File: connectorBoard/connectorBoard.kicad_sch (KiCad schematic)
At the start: 6 parts, among them J1 Conn_01x08_Female

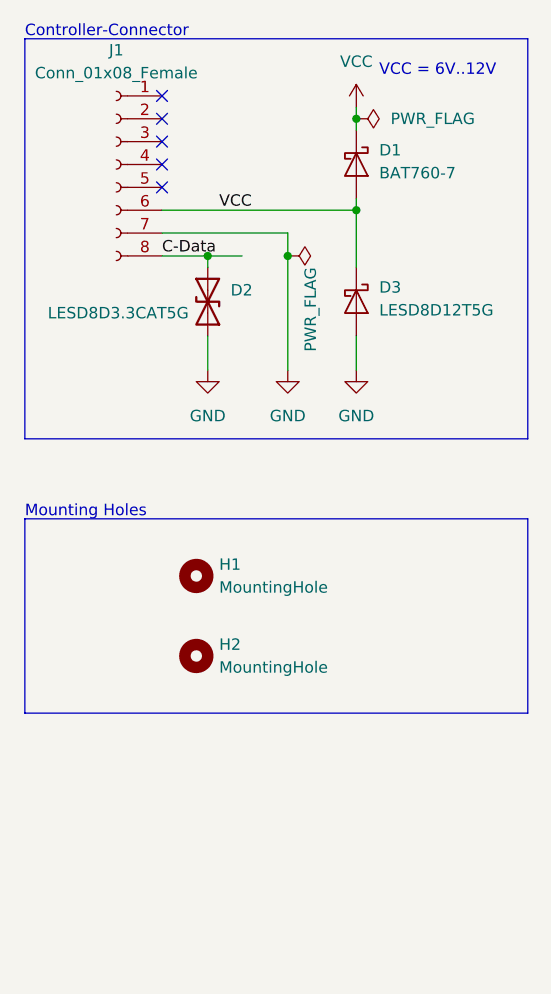
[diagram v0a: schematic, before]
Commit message: basic connector pcb design
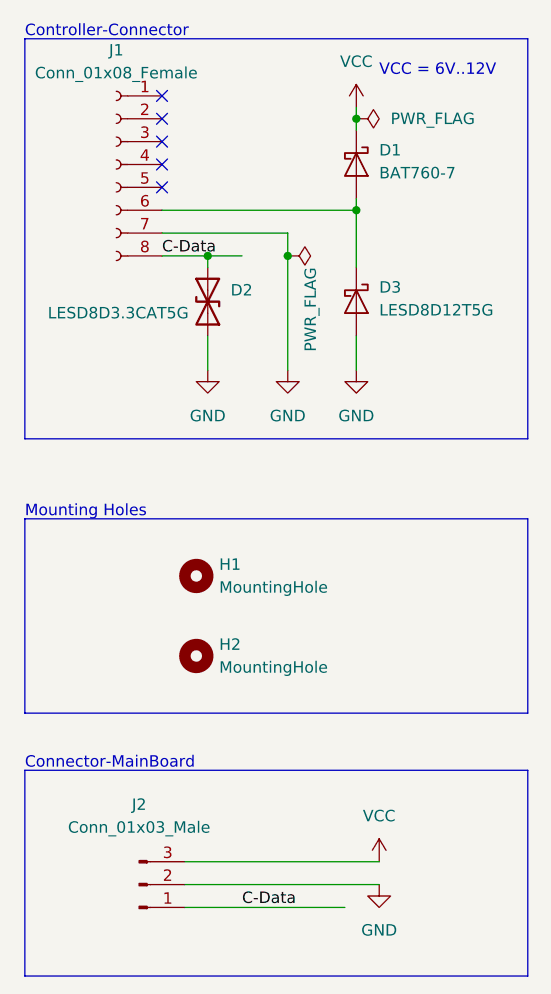
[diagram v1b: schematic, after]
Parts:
- added J2: Conn_01x03_Male, Connector_JST:JST_GH_SM03B-GHS-TB_1x03-1MP_P1.25mm_Horizontal, symbol Connector:Conn_01x03_Male
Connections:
- net C-Data: now also J2.1 (Pin_1)
- net GND: now also J2.2 (Pin_2)
- net VCC: now also J2.3 (Pin_3); no longer D1.2 (A), D3.1 (K), J1.6 (Pin_6)
- new net: D1.2 (A), D3.1 (K), J1.6 (Pin_6)
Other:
- note added: "Connector-MainBoard"
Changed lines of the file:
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@@
+    (stroke (width 0) (type default) (color 0 0 0 0))
+  )
+  (polyline (pts (xy 21.59 125.73) (xy 77.47 125.73))
     (stroke (width 0) (type default) (color 0 0 0 0))
   )
@@
     (stroke (width 0) (type default) (color 0 0 0 0))
   )
+  (polyline (pts (xy 77.47 125.73) (xy 77.47 102.87))
+    (stroke (width 0) (type default) (color 0 0 0 0))
+  )
   (wire (pts (xy 36.83 40.64) (xy 58.42 40.64))
     (stroke (width 0) (type default) (color 0 0 0 0))
   )
+  (wire (pts (xy 39.37 115.57) (xy 60.96 115.57))
+    (stroke (width 0) (type default) (color 0 0 0 0))
+  )
+  (polyline (pts (xy 21.59 102.87) (xy 77.47 102.87))
+    (stroke (width 0) (type default) (color 0 0 0 0))
+  )
+  (wire (pts (xy 39.37 113.03) (xy 60.96 113.03))
+    (stroke (width 0) (type default) (color 0 0 0 0))
+  )
   (wire (pts (xy 58.42 54.61) (xy 58.42 58.42))
     (stroke (width 0) (type default) (color 0 0 0 0))
   )
+  (wire (pts (xy 39.37 118.11) (xy 57.15 118.11))
+    (stroke (width 0) (type default) (color 0 0 0 0))
+  )
   (wire (pts (xy 41.91 54.61) (xy 41.91 58.42))
     (stroke (width 0) (type default) (color 0 0 0 0))
   )
+  (polyline (pts (xy 21.59 102.87) (xy 21.59 125.73))
+    (stroke (width 0) (type default) (color 0 0 0 0))
+  )
   (polyline (pts (xy 21.59 96.52) (xy 77.47 96.52))
     (stroke (width 0) (type default) (color 0 0 0 0))
@@
     (stroke (width 0) (type default) (color 0 0 0 0))
   )
+  (text "Connector-MainBoard\n" (at 21.59 102.87 0)
+    (effects (font (size 1.27 1.27)) (justify left bottom))
+  )
   (text "VCC = 6V..12V\n\n" (at 60.96 27.94 0)
     (effects (font (size 1.27 1.27)) (justify left bottom))
@@
     (effects (font (size 1.27 1.27)) (justify left bottom))
   )
-  (label "VCC" (at 43.18 40.64 0)
+  (label "C-Data" (at 45.72 118.11 0)
     (effects (font (size 1.27 1.27)) (justify left bottom))
   )
@@
     (pin "8")
   )
+  (symbol (lib_id "power:GND") (at 60.96 115.57 0) (unit 1)
+    (in_bom yes) (on_board yes) (fields_autoplaced)
+    (property "Reference" "#PWR0106" (id 0) (at 60.96 121.92 0)
+      (effects (font (size 1.27 1.27)) hide)
+    )
+    (property "Value" "GND" (id 1) (at 60.96 120.65 0))
+    (property "Footprint" "" (id 2) (at 60.96 115.57 0)
+      (effects (font (size 1.27 1.27)) hide)
+    )
+    (property "Datasheet" "" (id 3) (at 60.96 115.57 0)
+      (effects (font (size 1.27 1.27)) hide)
+    )
+    (pin "1")
+  )
   (symbol (lib_id "Mechanical:MountingHole") (at 40.64 90.17 0) (unit 1)
     (in_bom yes) (on_board yes) (fields_autoplaced)
@@
     (pin "1")
     (pin "2")
+  )
+  (symbol (lib_id "Connector:Conn_01x03_Male") (at 34.29 115.57 0) (mirror x) (unit 1)
+    (in_bom yes) (on_board yes)
+    (property "Reference" "J2" (id 0) (at 34.29 106.68 0))
+    (property "Value" "Conn_01x03_Male" (id 1) (at 34.29 109.22 0))
+    (property "Footprint" "Connector_JST:JST_GH_SM03B-GHS-TB_1x03-1MP_P1.25mm_Horizontal" (id 2) (at 34.29 115.57 0)
+      (effects (font (size 1.27 1.27)) hide)
+    )
+    (property "Datasheet" "~" (id 3) (at 34.29 115.57 0)
+      (effects (font (size 1.27 1.27)) hide)
+    )
+    (pin "1")
+    (pin "2")
+    (pin "3")
   )
   (symbol (lib_id "power:GND") (at 41.91 58.42 0) (unit 1)
@@
     (pin "1")
   )
-  (symbol (lib_id "Diode:PMEG1020EH") (at 58.42 35.56 270) (unit 1)
+  (symbol (lib_name "PMEG1020EH_1") (lib_id "Diode:PMEG1020EH") (at 58.42 35.56 270) (unit 1)
     (in_bom yes) (on_board yes) (fields_autoplaced)
     (property "Reference" "D1" (id 0) (at 60.96 33.9724 90)
@@
     )
     (property "Datasheet" "" (id 3) (at 58.42 58.42 0)
+      (effects (font (size 1.27 1.27)) hide)
+    )
+    (pin "1")
+  )
+  (symbol (lib_id "power:VCC") (at 60.96 113.03 0) (unit 1)
+    (in_bom yes) (on_board yes) (fields_autoplaced)
+    (property "Reference" "#PWR0105" (id 0) (at 60.96 116.84 0)
+      (effects (font (size 1.27 1.27)) hide)
+    )
+    (property "Value" "VCC" (id 1) (at 60.96 107.95 0))
+    (property "Footprint" "" (id 2) (at 60.96 113.03 0)
+      (effects (font (size 1.27 1.27)) hide)
+    )
+    (property "Datasheet" "" (id 3) (at 60.96 113.03 0)
       (effects (font (size 1.27 1.27)) hide)
     )
@@
       (reference "#PWR0104") (unit 1) (value "VCC") (footprint "")
     )
+    (path "/e57980bc-759f-45b8-a159-8a76488b5cdb"
+      (reference "#PWR0105") (unit 1) (value "VCC") (footprint "")
+    )
+    (path "/15697f34-2b14-48d2-8ad2-2408743b4505"
+      (reference "#PWR0106") (unit 1) (value "GND") (footprint "")
+    )
     (path "/809c85fe-6385-4f85-af32-063d785f40ce"
       (reference "D1") (unit 1) (value "BAT760-7") (footprint "Diode_SMD:D_SOD-323F")
@@
       (reference "J1") (unit 1) (value "Conn_01x08_Female") (footprint "Connector_PinSocket_2.54mm:PinSocket_1x08_P2.54mm_Vertical")
     )
-  )
+    (path "/4e980f01-8e3c-41e5-bc0e-00f4fc54f178"
+      (reference "J2") (unit 1) (value "Conn_01x03_Male") (footprint "Connector_JST:JST_GH_SM03B-GHS-TB_1x03-1MP_P1.25mm_Horizontal")
+    )
+  )
